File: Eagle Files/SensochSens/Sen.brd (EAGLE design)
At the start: 63.5 x 50.5 mm, 36 parts, among them U1 SM700PC1SMD, U2 MIC5219, X2 ADC0-7

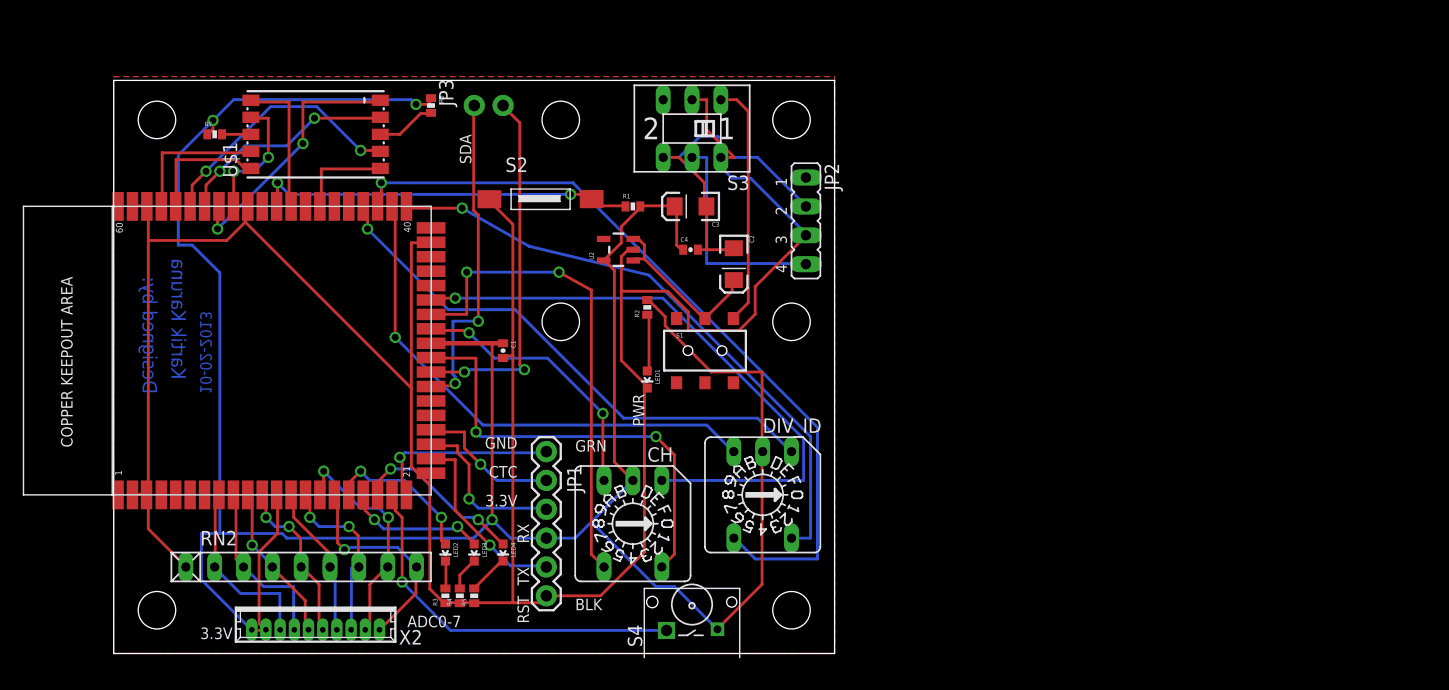
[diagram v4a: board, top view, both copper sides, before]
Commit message: 
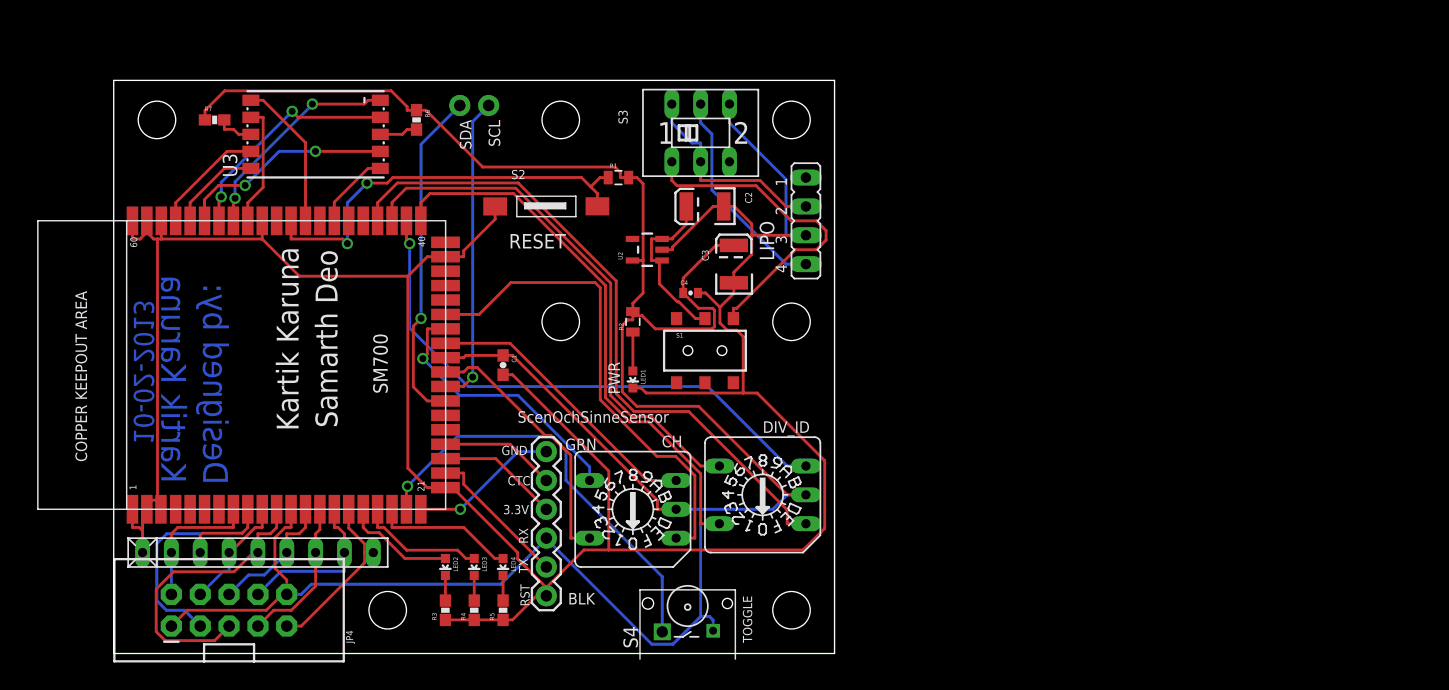
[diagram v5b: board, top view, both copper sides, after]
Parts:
- removed X2: ADC0-7, con-molex:53047-10
- added JP11: STAND-OFF, SparkFun:STAND-OFF
- C1: device SparkFun-Passives:0402-CAP -> SparkFun-Passives:0603-CAP
- C2, C3: device SparkFun-Passives:EIA3216 -> SparkFun-Passives:EIA3528
- CH, DIV_ID: value (none) -> HIX DIP
- JP2: value LIPO_charger -> LIPO
- JP4: value STAND-OFF -> M05X2SHD_LOCK; device SparkFun:STAND-OFF -> SparkFun-Connectors:2X5-SHROUDED_LOCK
- R1, R2: device SparkFun-Passives:0402-RES -> SparkFun-Passives:0805
- R3, R4, R5, R6, R7: device SparkFun-Passives:0402-RES -> SparkFun-Passives:0603-RES
- S1: value (none) -> Secondary sw
- S3: value (none) -> Primary sw
- moved JP5 61.4 mm to (59.7, 29.2)
- moved JP4 49.5 mm to (10.2, 3.81), turned to 90 degrees
- moved JP8 43.7 mm to (24.1, 3.81)
- moved JP7 43.2 mm to (59.7, 3.81)
- moved JP6 39.8 mm to (39.4, 29.2)
- moved JP9 35.6 mm to (3.81, 47.0)
- moved JP10 17.8 mm to (39.4, 47.0)
- moved C3 6.35 mm to (54.6, 34.3), turned to 90 degrees
- moved C2 5.68 mm to (52.1, 39.4), turned to 180 degrees
- moved RN2 4.02 mm to (12.7, 8.89)
- moved C4 3.81 mm to (50.8, 31.8)
- moved R5 2.84 mm to (34.3, 3.81)
- moved R1 2.84 mm to (44.5, 41.9)
- moved U2 2.54 mm to (47.0, 35.6)
- moved R2 1.80 mm to (45.7, 29.2)
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- renumbered U$1 to U3
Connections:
- net 3.3V: now also JP4.1, JP4.10; no longer X2.1, X2.2
- net ADC0: now also JP4.2; no longer X2.3
- net ADC1: now also JP4.3; no longer X2.4
- net ADC2: now also JP4.4; no longer X2.5
- net ADC3: now also JP4.5; no longer X2.6
- net ADC4: now also JP4.6; no longer X2.7
- net ADC5: now also JP4.7; no longer X2.8
- net ADC6: now also JP4.8; no longer X2.9
- net ADC7: now also JP4.9; no longer X2.10
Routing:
- net DIV_2: track 69.3 -> 46.9 mm, vias 1 -> 0
- net 3.3V: track 236.2 -> 217.3 mm, vias 3 -> 0
- net CH_2: track 43.1 -> 24.2 mm, vias 2 -> 1
- net CH_4: track 39.1 -> 23.4 mm, vias 2 -> 0
- net ADC3: track 14.8 -> 26.6 mm, vias 2 -> 0
- net DIV_1: track 47.6 -> 59.0 mm, vias 1 -> 0
- net CH_1: track 54.2 -> 43.1 mm, vias 1 -> 0
- net VCC1: track 21.6 -> 29.5 mm
- net ADC1: track 15.6 -> 23.2 mm
- net ADC6: track 20.4 -> 14.5 mm, vias 2 -> 0
- net SCL: track 32.3 -> 27.3 mm, vias 2 -> 1
- net DIV_4: track 53.4 -> 48.6 mm, vias 1 -> 0
- net TOGL: track 33.1 -> 37.8 mm
- net ADC7: track 19.2 -> 15.2 mm, vias 1 -> 0
- net RX2: track 14.7 -> 10.7 mm, vias 1 -> 0
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- removed copper zone on layer 1, net GND
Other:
- board text added: "SM700"
- board text added: "Samarth Deo"
- board text added: "ScenOchSinneSensor"
- board text removed: "A"
- board text removed: "B"
- board text removed: "C"
